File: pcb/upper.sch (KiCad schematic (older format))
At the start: 16 parts, among them J101 MALE, J102 FEMALE, J103 MALE, J104 FEMALE, J105 MALE, J106 FEMALE, J107 MALE, J108 FEMALE, J111 STANDOFF, J112 STANDOFF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

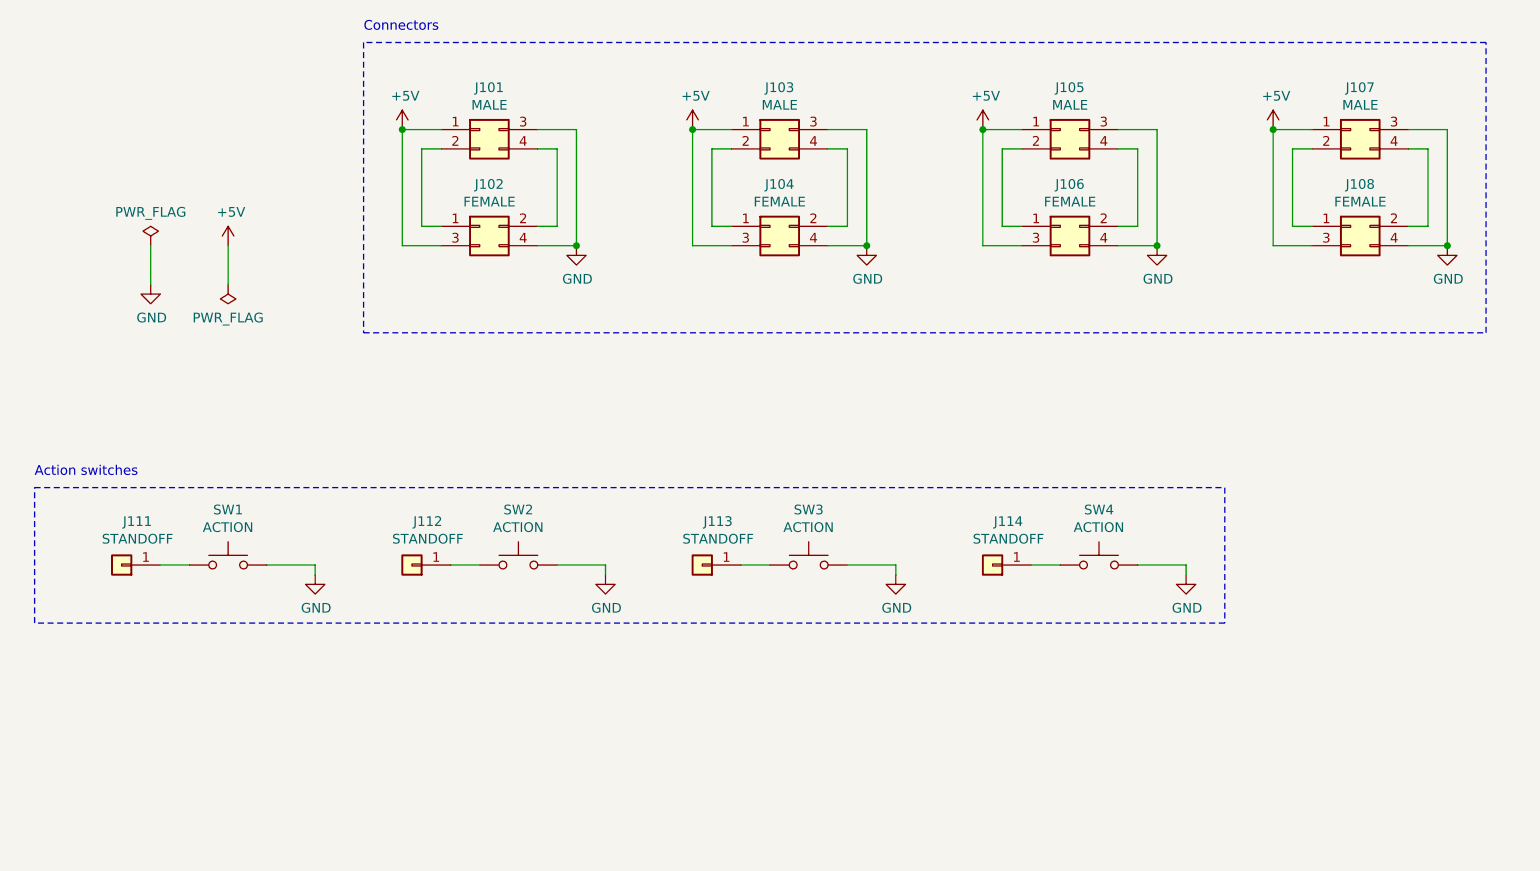
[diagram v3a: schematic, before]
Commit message: Fix bridging: Move male headers to upper board
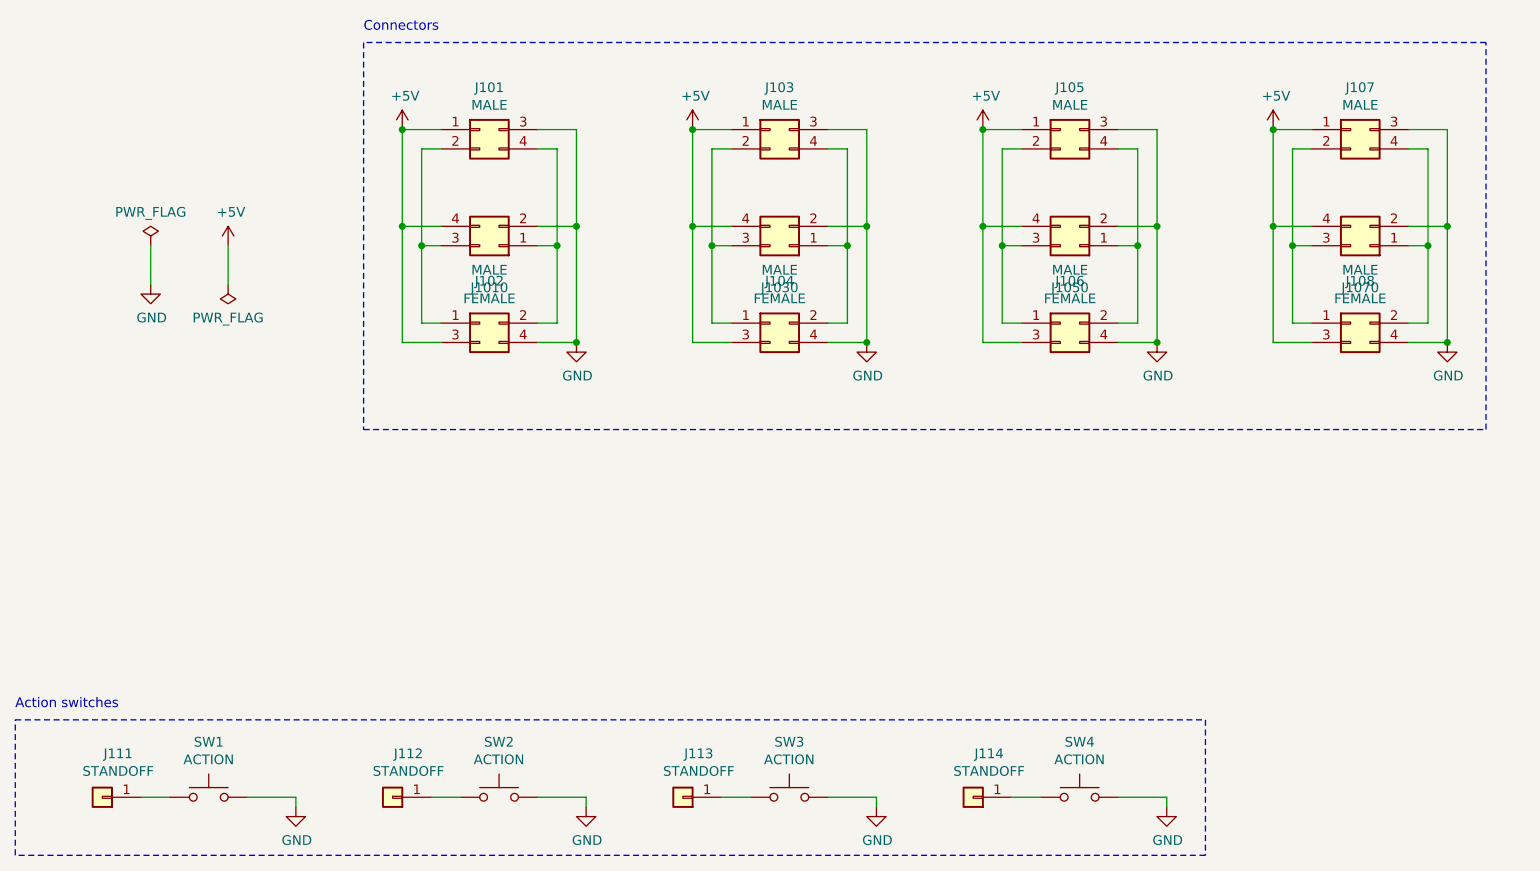
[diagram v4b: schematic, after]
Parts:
- added J1010, J1030, J1050, J1070: MALE, Connector_PinHeader_2.54mm:PinHeader_2x02_P2.54mm_Horizontal, symbol Connector_Generic:Conn_02x02_Top_Bottom
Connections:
- net +5V: now also J1010.4 (Pin_4), J1030.4 (Pin_4), J1050.4 (Pin_4), J1070.4 (Pin_4)
- net GND: now also J1010.2 (Pin_2), J1030.2 (Pin_2), J1050.2 (Pin_2), J1070.2 (Pin_2)
- net at J101.2 (Pin_2), J102.1 (Pin_1): now also J1010.3 (Pin_3)
- net at J101.4 (Pin_4), J102.2 (Pin_2): now also J1010.1 (Pin_1)
- net at J103.2 (Pin_2), J104.1 (Pin_1): now also J1030.3 (Pin_3)
- net at J103.4 (Pin_4), J104.2 (Pin_2): now also J1030.1 (Pin_1)
- net at J105.2 (Pin_2), J106.1 (Pin_1): now also J1050.3 (Pin_3)
- net at J105.4 (Pin_4), J106.2 (Pin_2): now also J1050.1 (Pin_1)
- net at J107.2 (Pin_2), J108.1 (Pin_1): now also J1070.3 (Pin_3)
- net at J107.4 (Pin_4), J108.2 (Pin_2): now also J1070.1 (Pin_1)
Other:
- moved on the sheet: J102, J104, J106, J108, J111, J112, J113, J114, SW1, SW2, SW3, SW4
